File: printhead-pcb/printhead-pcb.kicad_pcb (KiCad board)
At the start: 2 copper layers, 35 x 35 mm, 30 parts, among them J1 Power, J13 Steckverbinder_Male_1, J3 DATA, U1 PCA9615DP, U6 AP7361C-33E

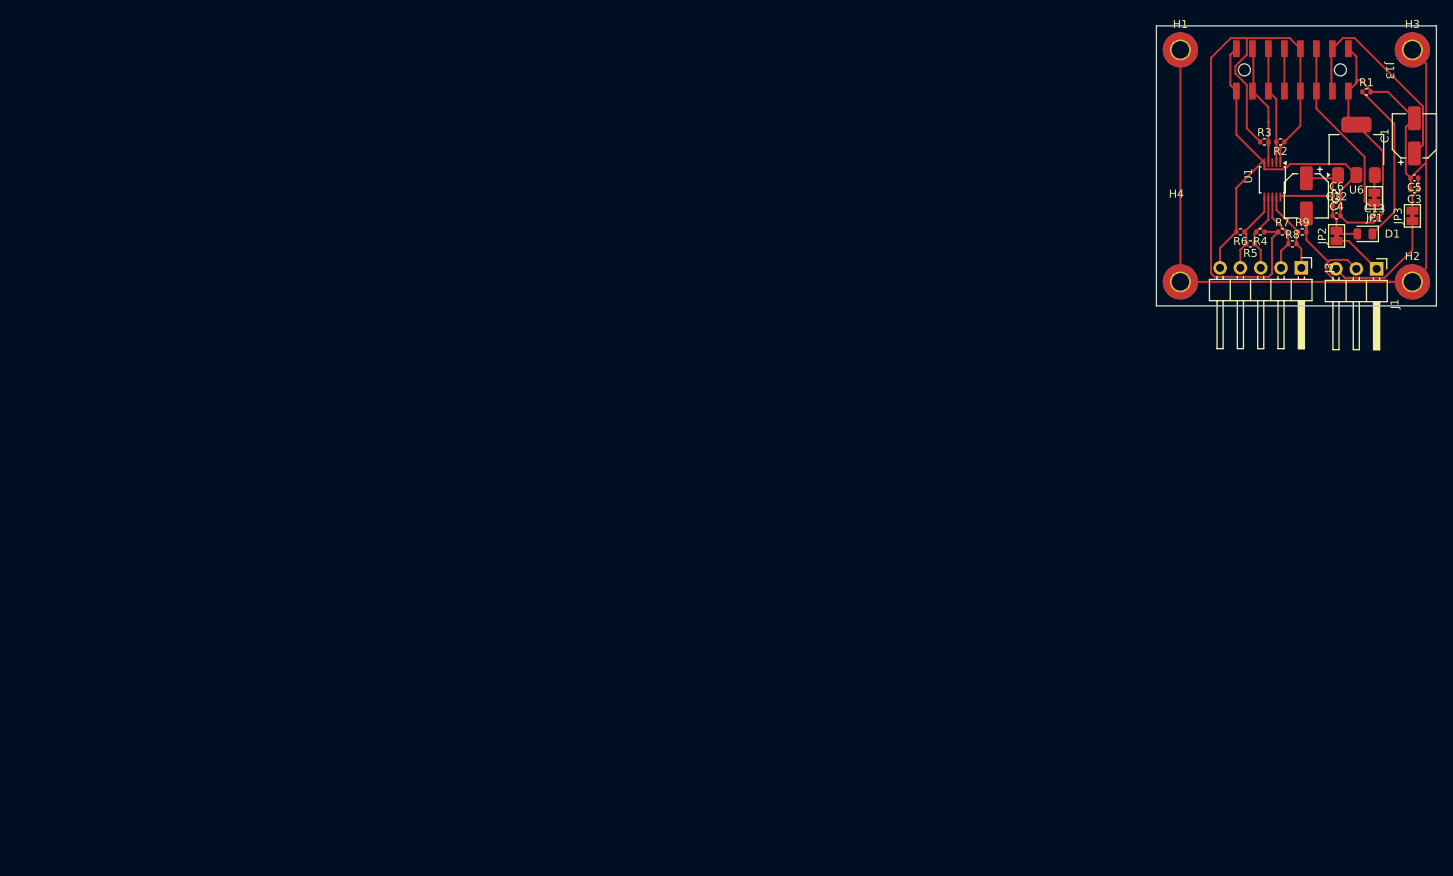
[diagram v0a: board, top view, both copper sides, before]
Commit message: alle module mal grob gemacht, beim ersten noch den gpio hinzugefuegt, leider nicht auf einer layerseite untergebracht
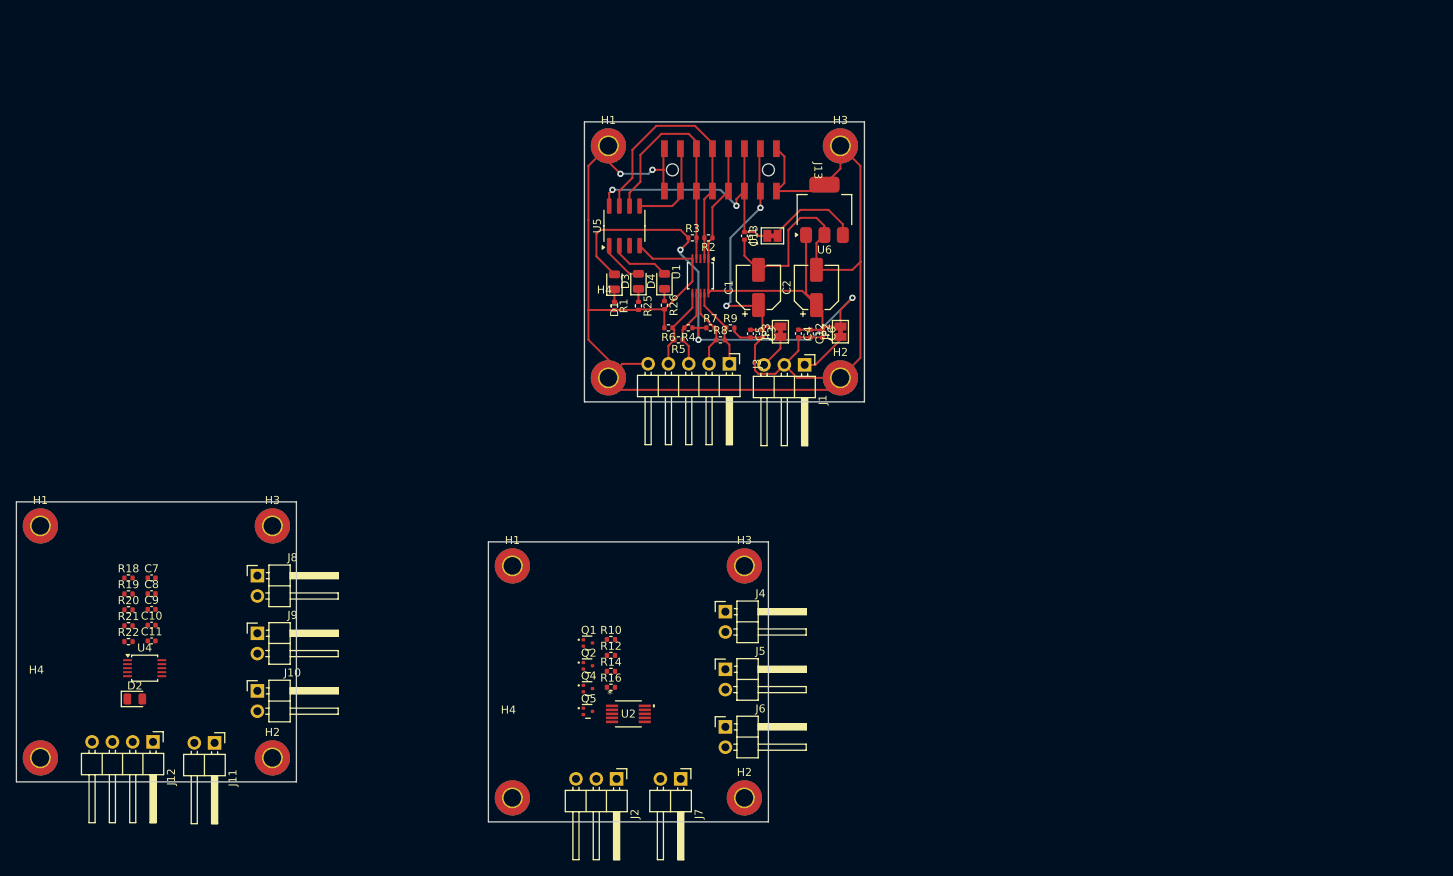
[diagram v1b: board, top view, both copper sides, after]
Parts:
- added C10: 0.1µF, Capacitor_SMD:C_0402_1005Metric, F.Cu at (89.9, 139.9)
- added C11: 0.1µF, Capacitor_SMD:C_0402_1005Metric, F.Cu at (89.9, 141.9)
- added C7: 0.1µF, Capacitor_SMD:C_0402_1005Metric, F.Cu at (89.9, 134.0)
- added C8: 0.1µF, Capacitor_SMD:C_0402_1005Metric, F.Cu at (89.9, 136.0)
- added C9: 0.1µF, Capacitor_SMD:C_0402_1005Metric, F.Cu at (89.9, 137.9)
- added D2: BLUE, LED_SMD:LED_0805_2012Metric, F.Cu at (87.8, 149.1)
- added D3: YELLOW, LED_SMD:LED_0805_2012Metric, F.Cu at (150.8, 96.9)
- added D4: YELLOW, LED_SMD:LED_0805_2012Metric, F.Cu at (154.0, 96.9)
- added H1: MountingHole_Pad, MountingHole:MountingHole_2.2mm_M2_Pad_TopBottom, F.Cu at (135.0, 132.5)
- added H1: MountingHole_Pad, MountingHole:MountingHole_2.2mm_M2_Pad_TopBottom, F.Cu at (76.0, 127.5)
- added H2: MountingHole_Pad, MountingHole:MountingHole_2.2mm_M2_Pad_TopBottom, F.Cu at (105.0, 156.5)
- added H2: MountingHole_Pad, MountingHole:MountingHole_2.2mm_M2_Pad_TopBottom, F.Cu at (164.0, 161.5)
- added H3: MountingHole_Pad, MountingHole:MountingHole_2.2mm_M2_Pad_TopBottom, F.Cu at (164.0, 132.5)
- added H3: MountingHole_Pad, MountingHole:MountingHole_2.2mm_M2_Pad_TopBottom, F.Cu at (105.0, 127.5)
- added H4: MountingHole_Pad, MountingHole:MountingHole_2.2mm_M2_Pad_TopBottom, F.Cu at (135.0, 161.5)
- added H4: MountingHole_Pad, MountingHole:MountingHole_2.2mm_M2_Pad_TopBottom, F.Cu at (76.0, 156.5)
- added J10: T2, Connector_PinHeader_2.54mm:PinHeader_1x02_P2.54mm_Horizontal, F.Cu at (103.1, 148.1)
- added J11: T3, Connector_PinHeader_2.54mm:PinHeader_1x02_P2.54mm_Horizontal, F.Cu at (97.8, 154.6)
- added J12: Breakout_Board_ADXL345, Connector_PinHeader_2.54mm:PinHeader_1x04_P2.54mm_Horizontal, F.Cu at (90.1, 154.5)
- added J2: Fan_12/5V_Regelung, Connector_PinHeader_2.54mm:PinHeader_1x03_P2.54mm_Horizontal, F.Cu at (148.0, 159.1)
- added J4: FAN0, Connector_PinHeader_2.54mm:PinHeader_1x02_P2.54mm_Horizontal, F.Cu at (161.6, 138.2)
- added J5: FAN1, Connector_PinHeader_2.54mm:PinHeader_1x02_P2.54mm_Horizontal, F.Cu at (161.6, 145.4)
- added J6: FAN2, Connector_PinHeader_2.54mm:PinHeader_1x02_P2.54mm_Horizontal, F.Cu at (161.6, 152.6)
- added J7: FAN4, Connector_PinHeader_2.54mm:PinHeader_1x02_P2.54mm_Horizontal, F.Cu at (156.0, 159.1)
- added J8: T0, Connector_PinHeader_2.54mm:PinHeader_1x02_P2.54mm_Horizontal, F.Cu at (103.1, 133.7)
- added J9: T1, Connector_PinHeader_2.54mm:PinHeader_1x02_P2.54mm_Horizontal, F.Cu at (103.1, 140.9)
- added Q1: DTC143E, Package_TO_SOT_SMD:SOT-723, F.Cu at (144.4, 142.1)
- added Q2: DTC143E, Package_TO_SOT_SMD:SOT-723, F.Cu at (144.4, 145.0)
- added Q4: DTC143E, Package_TO_SOT_SMD:SOT-723, F.Cu at (144.4, 147.8)
- added Q5: DTC143E, Package_TO_SOT_SMD:SOT-723, F.Cu at (144.4, 150.7)
- added R10: 4k7, Resistor_SMD:R_0402_1005Metric, F.Cu at (147.3, 141.7)
- added R12: 10k, Resistor_SMD:R_0402_1005Metric, F.Cu at (147.3, 143.7)
- added R14: 4k7, Resistor_SMD:R_0402_1005Metric, F.Cu at (147.3, 145.7)
- added R16: 4k7, Resistor_SMD:R_0402_1005Metric, F.Cu at (147.3, 147.7)
- added R18: 4k7, Resistor_SMD:R_0402_1005Metric, F.Cu at (87.0, 134.0)
- added R19: 4k7, Resistor_SMD:R_0402_1005Metric, F.Cu at (87.0, 136.0)
- added R20: 330, Resistor_SMD:R_0402_1005Metric, F.Cu at (87.0, 138.0)
- added R21: 4k7, Resistor_SMD:R_0402_1005Metric, F.Cu at (87.0, 140.0)
- added R22: 4k7, Resistor_SMD:R_0402_1005Metric, F.Cu at (87.0, 142.0)
- added R25: 330, Resistor_SMD:R_0402_1005Metric, F.Cu at (150.8, 100.0)
- added R26: 330, Resistor_SMD:R_0402_1005Metric, F.Cu at (154.0, 99.9)
- added U2: EMC2302-2-AIZL-TR, CustomFotLibByJan:MSOP10_MC_MCH, F.Cu at (149.5, 151.0)
- added U4: ADS1015IDGS, Package_SO:TSSOP-10_3x3mm_P0.5mm, F.Cu at (89.0, 145.3)
- added U5: PCA9536D, Package_SO:SOIC-8_3.9x4.9mm_P1.27mm, F.Cu at (149.0, 90.0)
- moved R1 97.7 mm to (147.8, 100.0), turned to -90 degrees
- moved D1 94.0 mm to (147.8, 97.0), turned to 90 degrees
- moved C5 85.2 mm to (164.8, 103.5), turned to -90 degrees
- moved C1 84.2 mm to (165.8, 97.7)
- moved C3 83.5 mm to (166.3, 103.5), turned to -90 degrees
- moved JP3 80.3 mm to (168.5, 103.2)
- moved C13 78.8 mm to (164.0, 91.2), turned to -90 degrees
- moved JP1 75.4 mm to (167.5, 91.2), turned to 180 degrees
- moved J13 72.6 mm to (168.0, 80.3)
- moved H1 72.5 mm to (147.0, 80.0)
- moved H2 72.5 mm to (176.0, 109.0)
- moved H3 72.5 mm to (176.0, 80.0)
- moved H4 72.5 mm to (147.0, 109.0)
- moved J1 72.5 mm to (171.5, 107.4)
- moved J3 72.5 mm to (162.1, 107.2)
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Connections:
- J13 pad a5: IO2 -> SDA
- J13 pad a6: SDA -> SCL
- J13 pad a7: SCL -> IO3
- J13 pad b5: IO2 -> SDA
- J13 pad b6: SDA -> SCL
- J13 pad b7: SCL -> IO3
- J3 pad 3: unconnected-(J3-Pin_3-Pad3) -> DSCLP
- J3 pad 4: unconnected-(J3-Pin_4-Pad4) -> DSCLM
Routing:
- net SDA: track 14.7 -> 34.7 mm
- net Net-(D1-K): track 20.6 -> 1.56 mm
- net SCL: track 15.2 -> 30.1 mm
- net IO3: track 0.00 -> 11.8 mm
- net Net-(J1-Pin_3): track 15.1 -> 4.35 mm
- net Net-(JP1-A): track 2.22 -> 11.8 mm
- net +3V3: track 24.9 -> 34.3 mm, vias 0 -> 2
- net IO1: track 0.00 -> 7.67 mm
- net +5V: track 106.0 -> 112.6 mm, vias 0 -> 3
- net IO0: track 0.00 -> 5.69 mm
- net IO2: track 5.30 -> 0.00 mm
- net Net-(D3-K): track 0.00 -> 1.61 mm
- net Net-(D4-K): track 0.00 -> 1.54 mm
- net +12V: track 31.5 -> 32.8 mm, vias 0 -> 2
- net GND: track 218.3 -> 217.1 mm, vias 0 -> 2
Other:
- board size 35 x 35 mm -> 106 x 87.5 mm

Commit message: removed gpio, design with only one layer AND short and almost equally long data routes
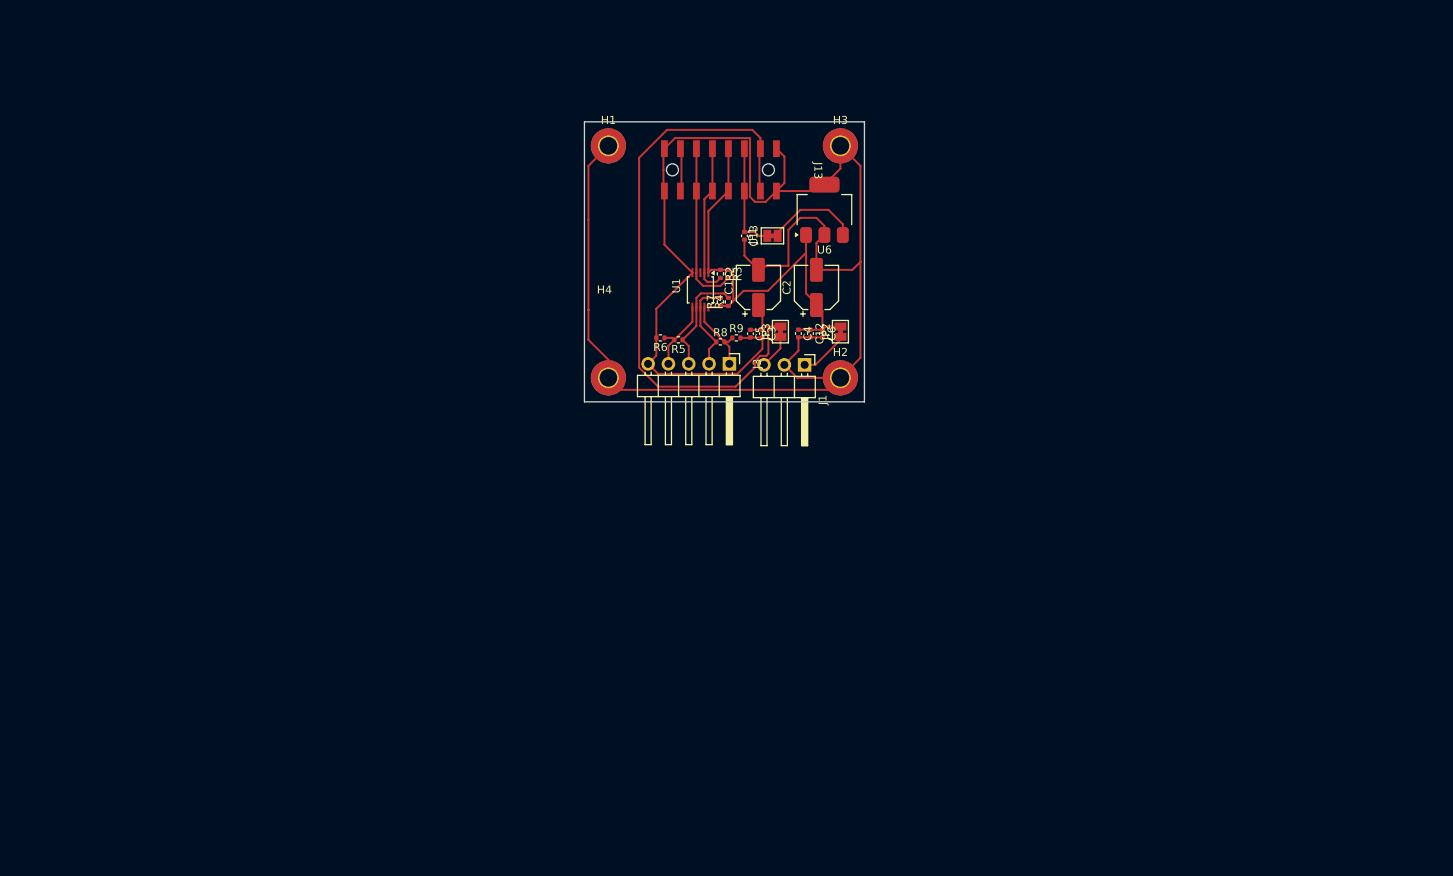
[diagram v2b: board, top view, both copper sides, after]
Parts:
- removed C10, C11, C7, C8, C9: 0.1µF, Capacitor_SMD:C_0402_1005Metric
- removed D1: GREEN, LED_SMD:LED_0805_2012Metric
- removed D2: BLUE, LED_SMD:LED_0805_2012Metric
- removed D3, D4: YELLOW, LED_SMD:LED_0805_2012Metric
- removed the H1 at (135.0, 132.5)
- removed the H1 at (76.0, 127.5)
- removed the H2 at (105.0, 156.5)
- removed the H2 at (164.0, 161.5)
- removed the H3 at (164.0, 132.5)
- removed the H3 at (105.0, 127.5)
- removed the H4 at (135.0, 161.5)
- removed the H4 at (76.0, 156.5)
- removed J10: T2, Connector_PinHeader_2.54mm:PinHeader_1x02_P2.54mm_Horizontal
- removed J11: T3, Connector_PinHeader_2.54mm:PinHeader_1x02_P2.54mm_Horizontal
- removed J12: Breakout_Board_ADXL345, Connector_PinHeader_2.54mm:PinHeader_1x04_P2.54mm_Horizontal
- removed J2: Fan_12/5V_Regelung, Connector_PinHeader_2.54mm:PinHeader_1x03_P2.54mm_Horizontal
- removed J4: FAN0, Connector_PinHeader_2.54mm:PinHeader_1x02_P2.54mm_Horizontal
- removed J5: FAN1, Connector_PinHeader_2.54mm:PinHeader_1x02_P2.54mm_Horizontal
- removed J6: FAN2, Connector_PinHeader_2.54mm:PinHeader_1x02_P2.54mm_Horizontal
- removed J7: FAN4, Connector_PinHeader_2.54mm:PinHeader_1x02_P2.54mm_Horizontal
- removed J8: T0, Connector_PinHeader_2.54mm:PinHeader_1x02_P2.54mm_Horizontal
- removed J9: T1, Connector_PinHeader_2.54mm:PinHeader_1x02_P2.54mm_Horizontal
- removed Q1, Q2, Q4, Q5: DTC143E, Package_TO_SOT_SMD:SOT-723
- removed R1: 1k, Resistor_SMD:R_0402_1005Metric
- removed R10, R14, R16, R18, R19, R21, R22: 4k7, Resistor_SMD:R_0402_1005Metric
- removed R12: 10k, Resistor_SMD:R_0402_1005Metric
- removed R20, R25, R26: 330, Resistor_SMD:R_0402_1005Metric
- removed U2: EMC2302-2-AIZL-TR, CustomFotLibByJan:MSOP10_MC_MCH
- removed U4: ADS1015IDGS, Package_SO:TSSOP-10_3x3mm_P0.5mm
- removed U5: PCA9536D, Package_SO:SOIC-8_3.9x4.9mm_P1.27mm
- moved R3 6.36 mm to (162.0, 96.0), turned to -90 degrees
- moved R4 5.96 mm to (162.0, 99.5), turned to 90 degrees
- moved R2 4.75 mm to (161.0, 96.0), turned to -90 degrees
- moved R7 3.48 mm to (161.0, 99.5), turned to 90 degrees
- moved U1 1.76 mm to (158.5, 98.0)
- moved R6 1.61 mm to (153.5, 104.0)
- moved R9 1.46 mm to (163.0, 104.0)
- moved R8 0.26 mm to (161.0, 104.5)
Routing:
- net +5V: track 112.6 -> 58.7 mm, vias 3 -> 0
- net +12V: track 32.8 -> 81.4 mm, vias 2 -> 0
- net +3V3: track 34.3 -> 13.5 mm, vias 2 -> 0
- net SDA: track 34.7 -> 19.1 mm
- net GND: track 217.1 -> 232.1 mm, vias 2 -> 0
- net SCL: track 30.1 -> 21.1 mm
- net IO1: track 7.67 -> 0.00 mm
- net IO3: track 11.8 -> 5.40 mm
- net IO0: track 5.69 -> 0.00 mm
- net DSCLP: track 9.89 -> 13.7 mm
- net DSDAP: track 10.1 -> 11.7 mm
- net Net-(D3-K): track 1.61 -> 0.00 mm
- net Net-(D1-K): track 1.56 -> 0.00 mm
- net Net-(D4-K): track 1.54 -> 0.00 mm
- net DSDAM: track 10.3 -> 9.58 mm
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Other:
- board size 106 x 87.5 mm -> 35 x 35 mm

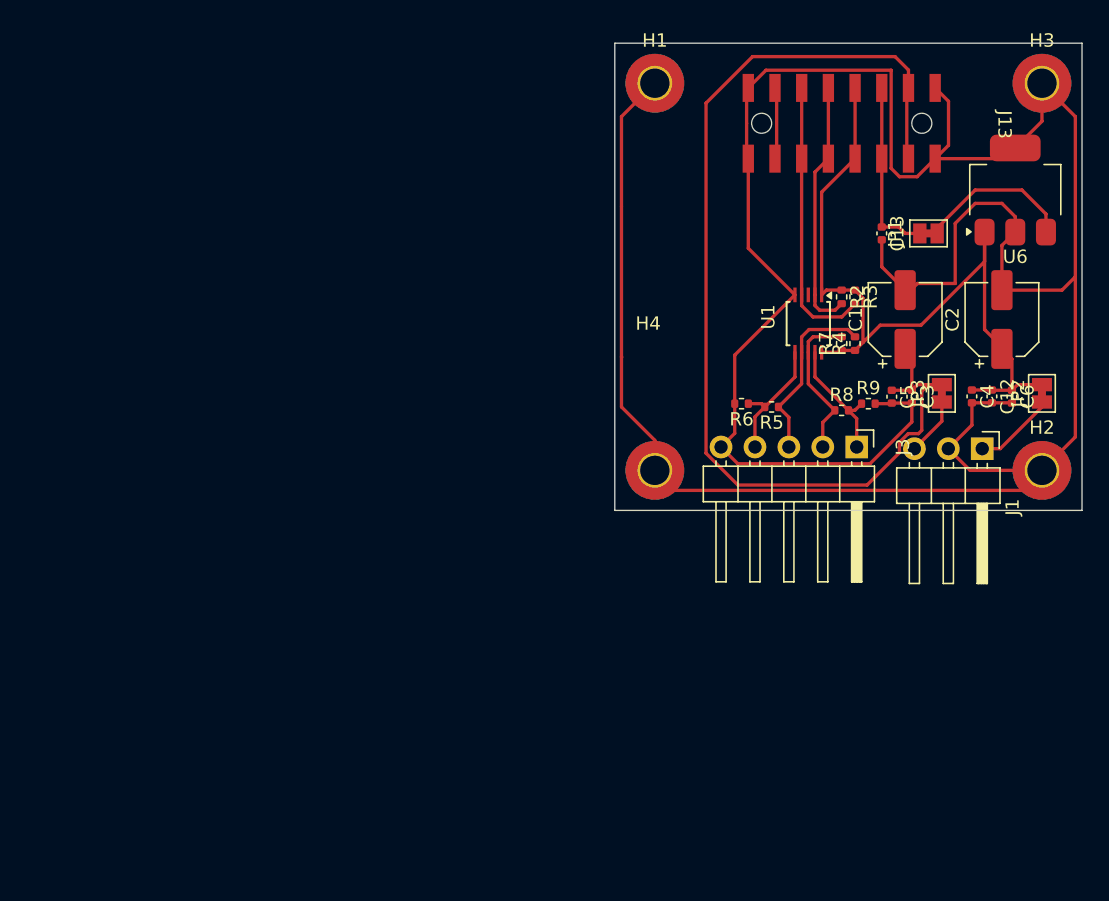
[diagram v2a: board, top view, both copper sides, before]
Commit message: very good layout, now reajusting the postions just a bit and making the traces thicker
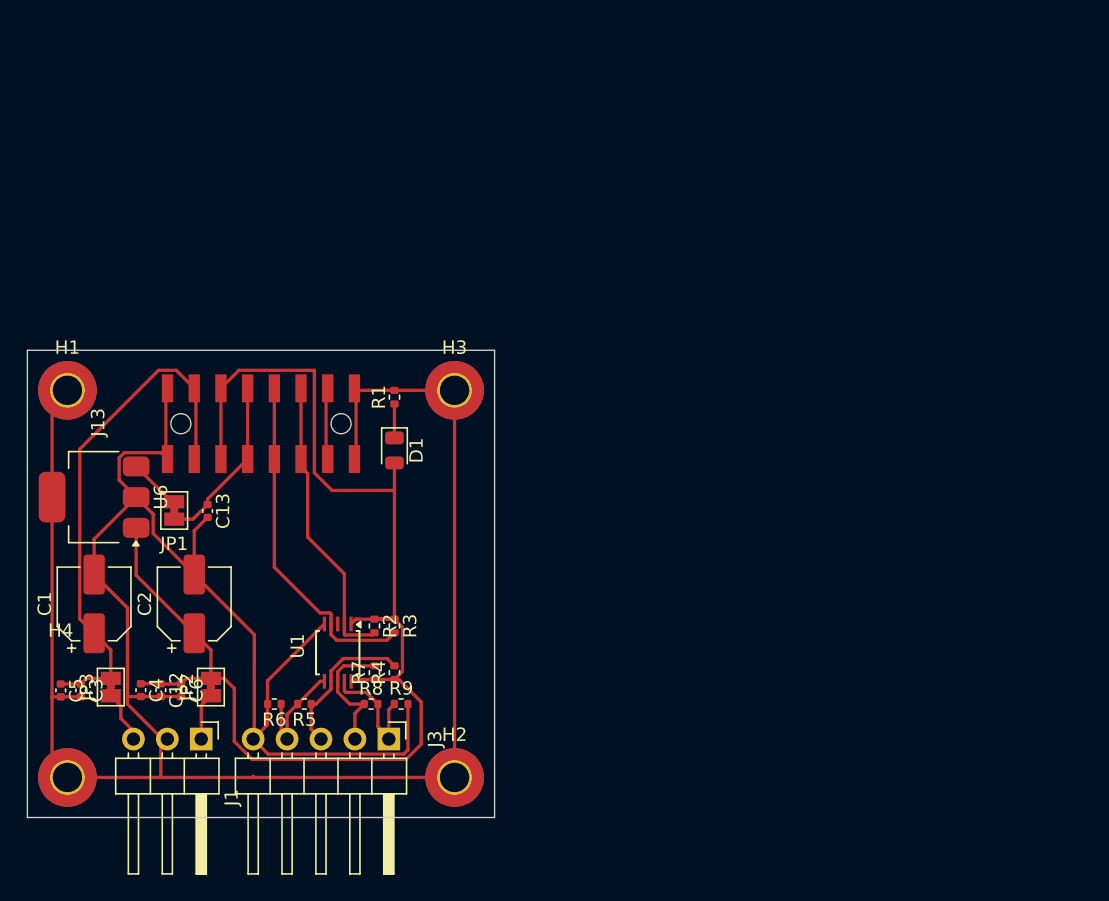
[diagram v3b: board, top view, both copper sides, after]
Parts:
- added D1: GREEN, LED_SMD:LED_0805_2012Metric, F.Cu at (127.5, 107.5)
- added R1: 1k, Resistor_SMD:R_0402_1005Metric, F.Cu at (127.5, 103.5)
- moved U6 72.7 mm to (105.0, 111.0), turned to 180 degrees
- moved C12 66.0 mm to (110.0, 125.5)
- moved C3 66.0 mm to (104.0, 125.5)
- moved C4 66.0 mm to (108.5, 125.5)
- moved C5 66.0 mm to (102.5, 125.5)
- moved C6 66.0 mm to (111.5, 125.5)
- moved JP2 66.0 mm to (113.8, 125.2)
- moved JP3 66.0 mm to (106.2, 125.2)
- moved C1 64.4 mm to (105.0, 119.0)
- moved C2 64.1 mm to (112.5, 119.0)
- moved J13 63.9 mm to (110.5, 108.2), turned to 90 degrees
- moved J1 62.4 mm to (113.0, 129.1)
- moved JP1 60.2 mm to (111.0, 112.0), turned to -90 degrees
- moved C13 54.6 mm to (113.5, 112.0)
- moved H1 49.7 mm to (103.0, 103.0)
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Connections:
- J13 pad a3: +3V3 -> +5V
- J13 pad a4: +5V -> +3V3
- J13 pad a5: SDA -> SCL
- J13 pad a6: SCL -> SDA
- J13 pad b3: +3V3 -> +5V
- J13 pad b4: +5V -> +3V3
- J13 pad b5: SDA -> SCL
- J13 pad b6: SCL -> SDA
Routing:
- net +12V: track 81.4 -> 39.0 mm
- net +5V: track 58.7 -> 98.3 mm
- net GND: track 232.1 -> 197.8 mm
- net Net-(JP1-A): track 11.8 -> 3.95 mm
- net SCL: track 21.1 -> 25.8 mm
- net SDA: track 19.1 -> 22.1 mm
- net Net-(J1-Pin_1): track 6.14 -> 3.55 mm
- net Net-(D1-K): track 0.00 -> 2.54 mm
- net DSCLP: track 13.7 -> 11.6 mm
- net DSDAP: track 11.7 -> 9.73 mm
- net DSCLM: track 9.68 -> 8.47 mm
- net +3V3: track 13.5 -> 12.9 mm
